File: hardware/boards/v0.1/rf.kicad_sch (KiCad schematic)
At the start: 6 parts, among them SW23 RST, U41 ME16WS03, U42 nRF

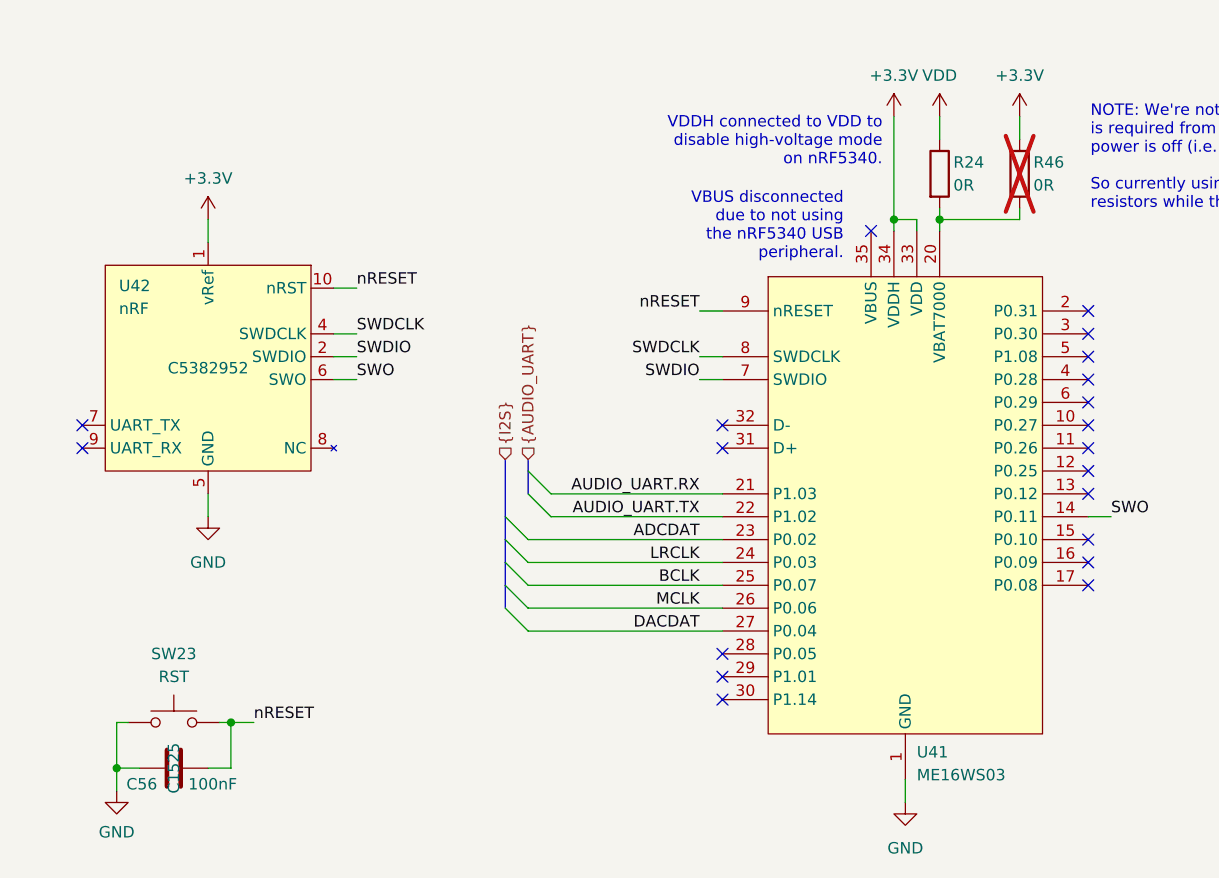
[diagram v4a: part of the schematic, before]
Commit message: feat: various routing cleanup, add SD flash
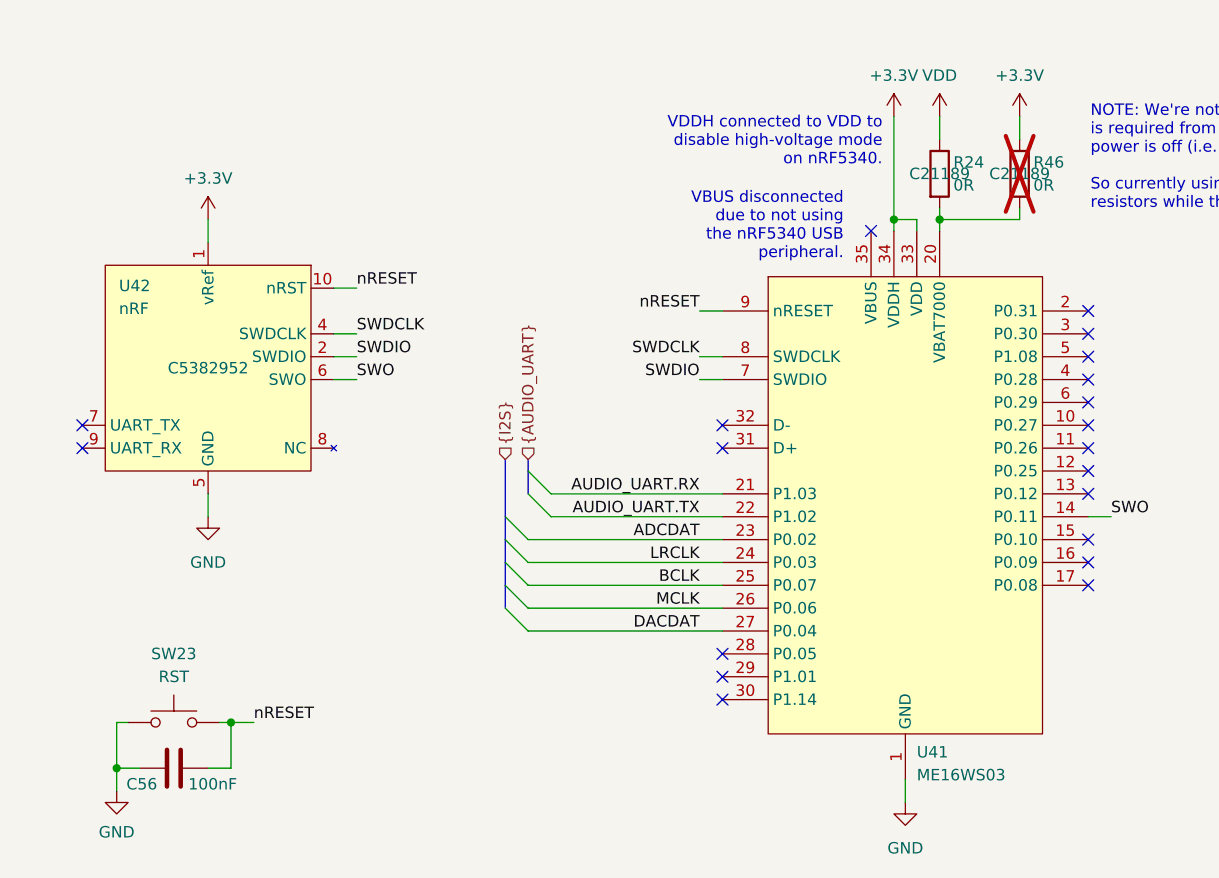
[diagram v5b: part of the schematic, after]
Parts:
- C56: footprint Capacitor_SMD:C_0603_1608Metric -> Capacitor_SMD:C_0402_1005Metric
- R24, R46: JLC (none) -> C21189
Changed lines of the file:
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@@
+			)
+		)
+		(property "Part" ""
+			(at 55.88 133.35 0)
+			(effects
+				(font
+					(size 1.27 1.27)
+				)
 			)
 		)
@@
 			)
 		)
+		(property "Part" ""
+			(at 137.16 109.22 0)
+			(effects
+				(font
+					(size 1.27 1.27)
+				)
+			)
+		)
 		(pin "16"
 		)
@@
 				)
 				(hide yes)
+			)
+		)
+		(property "JLC" "C21189"
+			(at 140.97 72.39 0)
+			(effects
+				(font
+					(size 1.27 1.27)
+				)
+			)
+		)
+		(property "Part" ""
+			(at 140.97 72.39 0)
+			(effects
+				(font
+					(size 1.27 1.27)
+				)
 			)
 		)
@@
 			)
 		)
-		(property "Footprint" "Capacitor_SMD:C_0603_1608Metric"
+		(property "Footprint" "Capacitor_SMD:C_0402_1005Metric"
 			(at 59.69 137.4648 0)
 			(effects
@@
 		)
 		(property "JLC" "C1525"
+			(at 55.88 138.43 0)
+			(effects
+				(font
+					(size 1.27 1.27)
+				)
+				(hide yes)
+			)
+		)
+		(property "Part" ""
 			(at 55.88 138.43 0)
 			(effects
@@
 			)
 		)
+		(property "JLC" "C21189"
+			(at 149.86 72.39 0)
+			(effects
+				(font
+					(size 1.27 1.27)
+				)
+			)
+		)
+		(property "Part" ""
+			(at 149.86 72.39 0)
+			(effects
+				(font
+					(size 1.27 1.27)
+				)
+			)
+		)
 		(pin "2"
 		)
@@
 			(at 59.69 93.98 0)
 			(effects
+				(font
+					(size 1.27 1.27)
+				)
+			)
+		)
+		(property "Part" ""
+			(at 59.69 93.98 0)
+			(effects

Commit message: chore: more schematic and routing organization
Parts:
- SW23: now not fitted; now left out of the parts list
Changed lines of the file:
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@@
 		(unit 1)
 		(exclude_from_sim no)
-		(in_bom yes)
+		(in_bom no)
 		(on_board yes)
-		(dnp no)
+		(dnp yes)
 		(fields_autoplaced yes)
 		(property "Reference" "SW23"

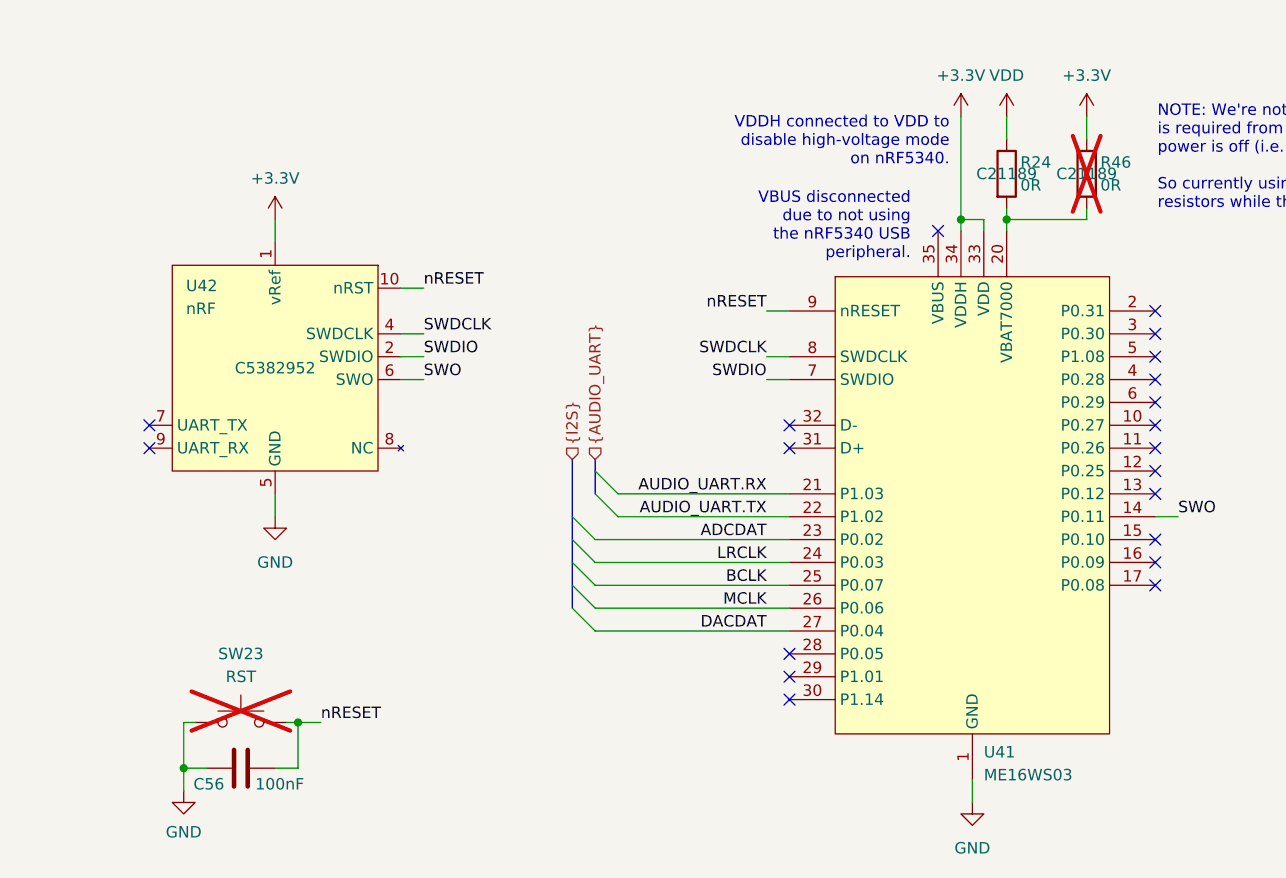
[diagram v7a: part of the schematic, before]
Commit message: feat: add haptic transducer DAC
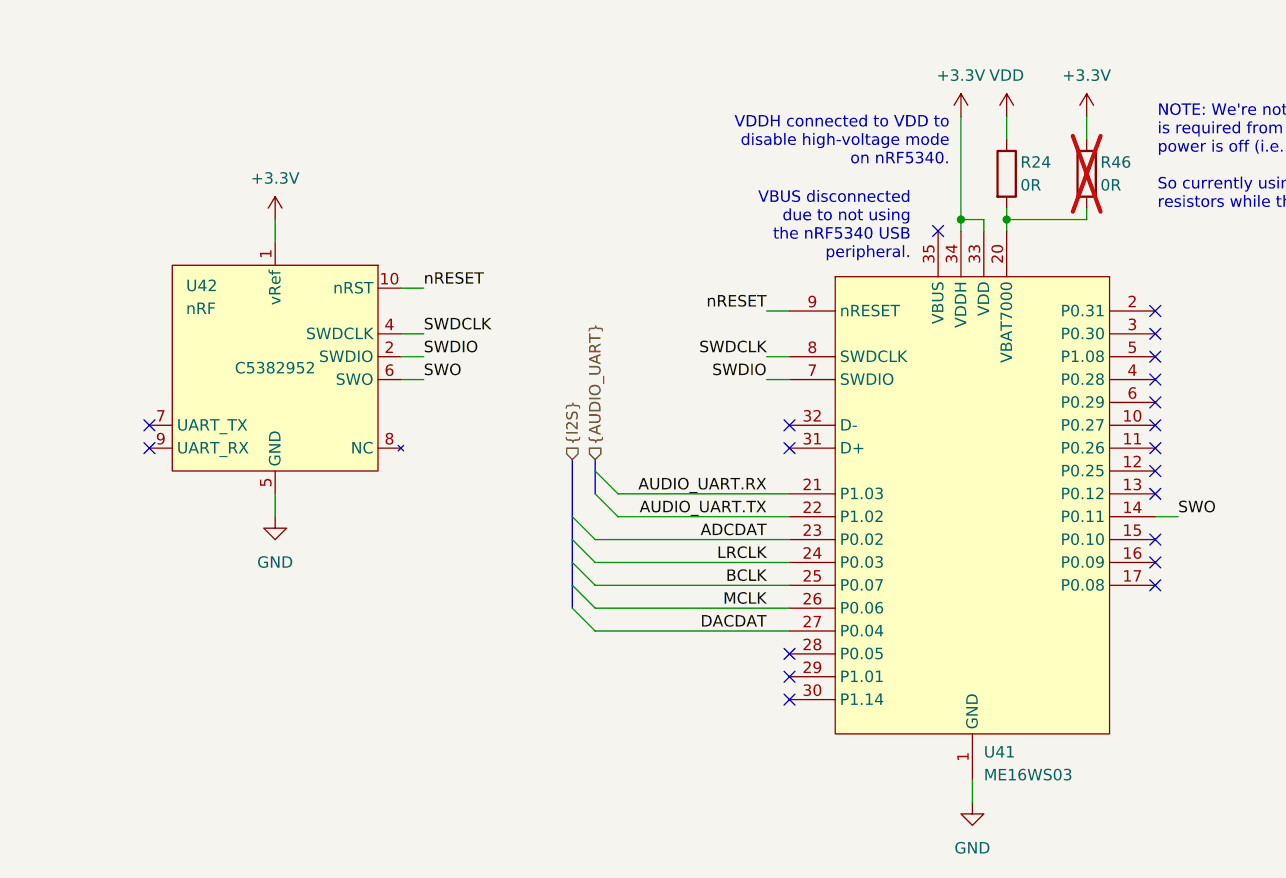
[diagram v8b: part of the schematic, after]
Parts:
- removed C56: 100nF, Capacitor_SMD:C_0402_1005Metric, symbol Device:C
- removed SW23: RST, Button_Switch_SMD:SW_SPST_B3U-1000P, symbol Switch:SW_Push
